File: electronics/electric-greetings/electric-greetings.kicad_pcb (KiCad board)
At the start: 2 copper layers, 12 x 30 mm, 17 parts, among them Q1 ALS-PT19-315C, SW1 B3U-1000P_SPST-NO_SMD, U1 ATSAMD21E18A, U2 AP2112K-3.3, U3 APA102-2020

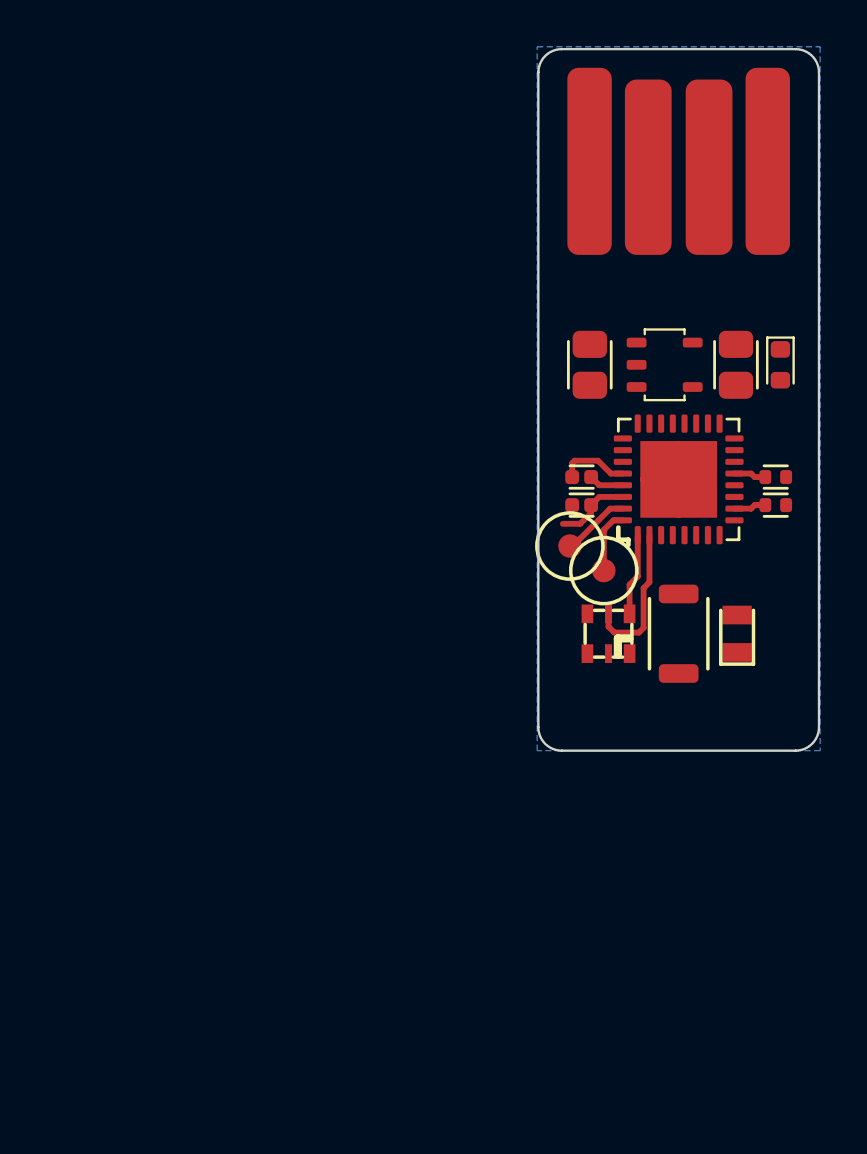
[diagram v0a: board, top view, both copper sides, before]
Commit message: Schematic tweaks, placement changes, routing
Most routing done, added capacitive buttons, remapped micro pins slightly.
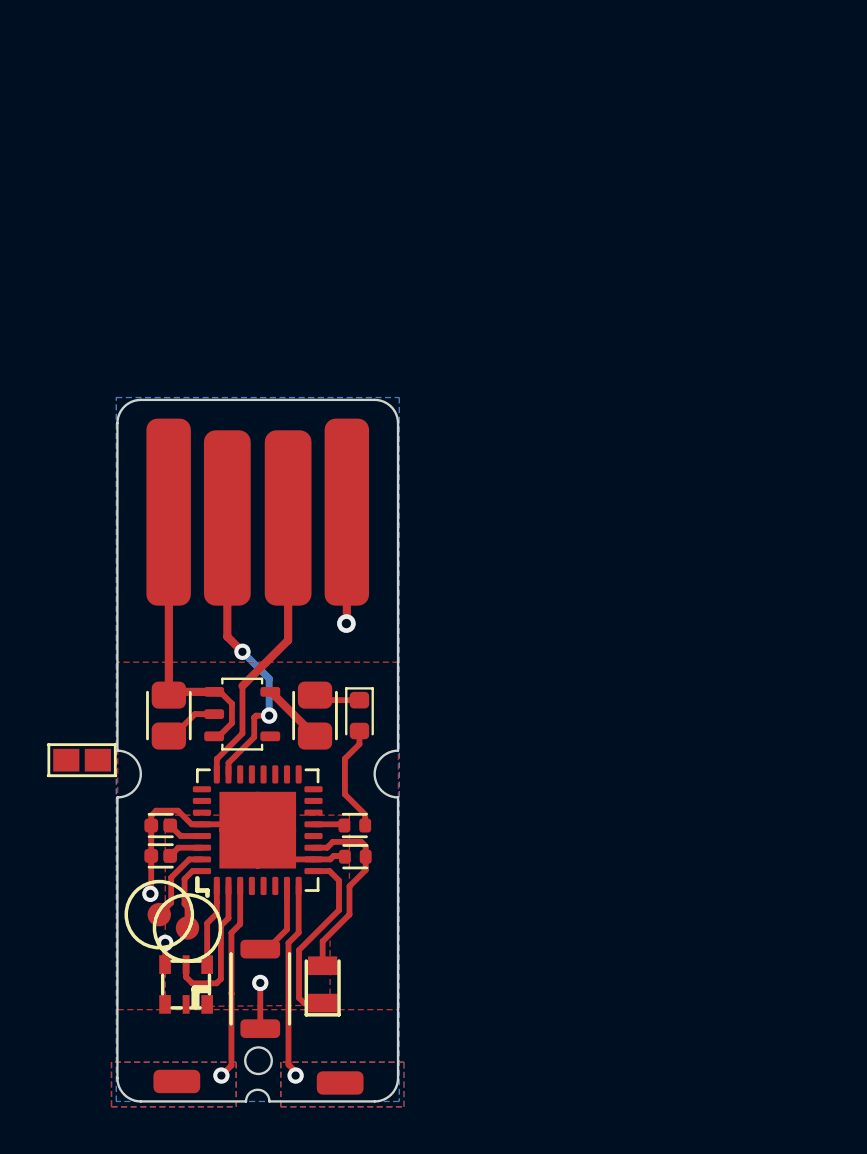
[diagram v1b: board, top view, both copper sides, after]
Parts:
- added P1: PAD_SOLDER_2mm, Applidyne_Connector:PAD_SOLDER_2mm, F.Cu at (102.5, 99.1)
- added P2: PAD_SOLDER_2mm, Applidyne_Connector:PAD_SOLDER_2mm, F.Cu at (109.5, 99.2)
- added SL1: SOLDER-LINK-2, Applidyne_Link:SJ1608-2N, F.Cu at (98.5, 85.4)
- moved LOGO1 24.2 mm to (106.0, 89.2)
- moved TEST1 23.6 mm to (101.8, 92.0)
- moved U3 23.5 mm to (102.9, 95.0)
- moved SW1 23.5 mm to (106.1, 95.2), turned to 270 degrees
- moved TEST2 23.5 mm to (103.0, 92.6)
- moved U2 23.4 mm to (105.3, 83.4)
- moved R2 23.4 mm to (110.2, 89.5)
- moved C1 23.4 mm to (101.8, 89.5)
- moved C3 23.4 mm to (102.2, 83.5)
- moved C4 23.4 mm to (108.5, 83.5), turned to 90 degrees
- moved D1 23.4 mm to (110.3, 83.5)
- moved J?1 23.4 mm to (106.0, 69.9)
- moved LOGO4 23.4 mm to (106.0, 74.8)
- moved U1 23.4 mm to (106.0, 88.4)
- moved C2 23.4 mm to (101.8, 88.2)
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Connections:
- SW1 pad 2: RESET -> USER_BUTTON
- U1 pad : (no net) -> GND
- U1 pad 11: Net-(U1-Pad11) -> PHOTOSENSOR
- U1 pad 3: Net-(U1-Pad3) -> TOUCH_A
- U1 pad 7: PHOTOSENSOR -> USER_BUTTON
- U1 pad 8: CURRENT -> TOUCH_B
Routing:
- net GND: track 4.42 -> 23.0 mm, vias 0 -> 4
- net USB_D-: track 0.00 -> 12.8 mm, vias 0 -> 2
- net VCC: track 0.00 -> 12.7 mm
- net USB_D+: track 0.00 -> 12.2 mm
- net +3.3V: track 3.24 -> 12.7 mm
- net TOUCH_A: track 0.00 -> 8.46 mm, vias 0 -> 1
- net TOUCH_B: track 0.00 -> 8.41 mm, vias 0 -> 1
- net PHOTOSENSOR: track 0.00 -> 8.28 mm
- net Net-(D1-PadA): track 0.00 -> 4.66 mm
- net USER_BUTTON: track 0.00 -> 3.35 mm
- net SWD_CLK: track 2.93 -> 3.43 mm
- added copper zone on F.Cu, net +3.3V
- added copper zone on B.Cu, net TOUCH_A
- added copper zone on F.Cu, net TOUCH_A
- added copper zone on B.Cu, net TOUCH_B
- added copper zone on F.Cu, net TOUCH_B
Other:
- outline, holes or cut-outs redrawn

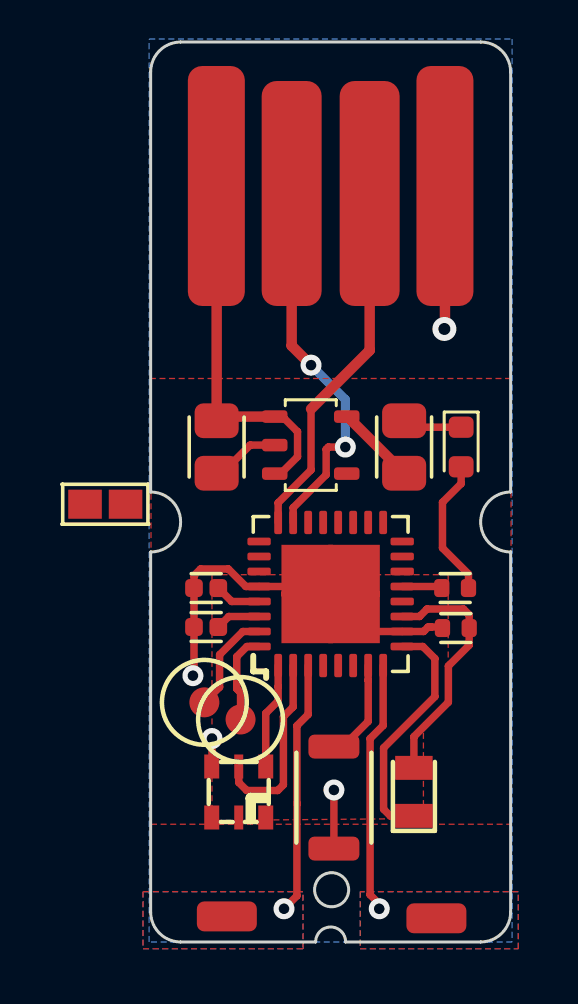
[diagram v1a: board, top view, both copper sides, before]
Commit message: More minor tweaks, finished all routing
Most cosmetics finished, just iterating on useless details now
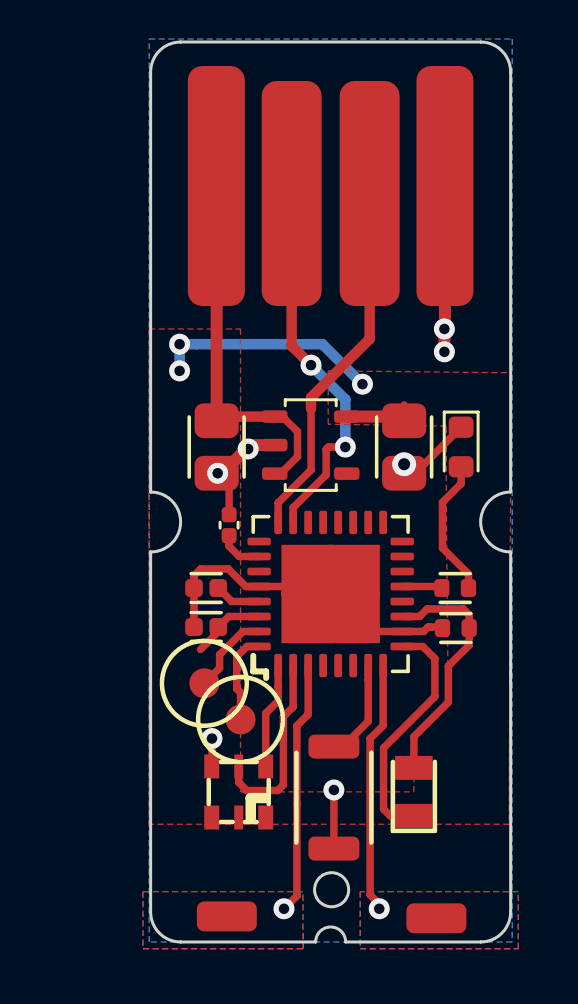
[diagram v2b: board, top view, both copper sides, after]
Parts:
- SL1: value SOLDER-LINK-2 -> SOLDER-LINK-2-TINY; footprint Applidyne_Link:SJ1608-2N -> Applidyne_Link:SJ1005-2N
- moved SL1 4.19 mm to (102.6, 86.1), turned to 270 degrees
- moved TEST1 0.64 mm to (101.8, 91.4)
- turned C4 to 270 degrees
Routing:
- net +3.3V: track 12.7 -> 21.1 mm, vias 0 -> 3
- net GND: track 23.0 -> 27.5 mm, vias 4 -> 7
- net RESET: track 0.00 -> 1.49 mm
- net SWD_CLK: track 3.43 -> 2.80 mm

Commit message: Removed usb logo
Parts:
- removed LOGO4: LOGO, Applidyne_Logo:USB_LOGO410X250
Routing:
- net GND: track 27.5 -> 30.1 mm, vias 7 -> 8
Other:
- board text added: "eui.io"
- board text removed: "try.eui.io"

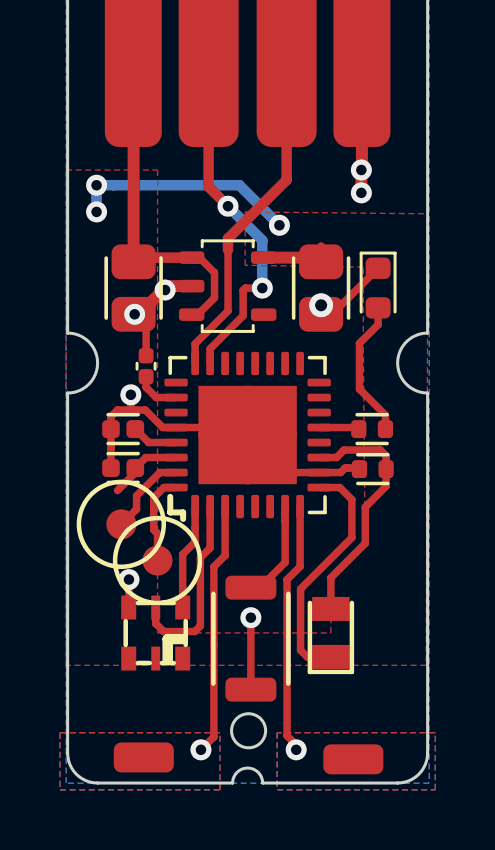
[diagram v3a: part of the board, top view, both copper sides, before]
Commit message: Fixed SWD programming points with 1mm pad footprint
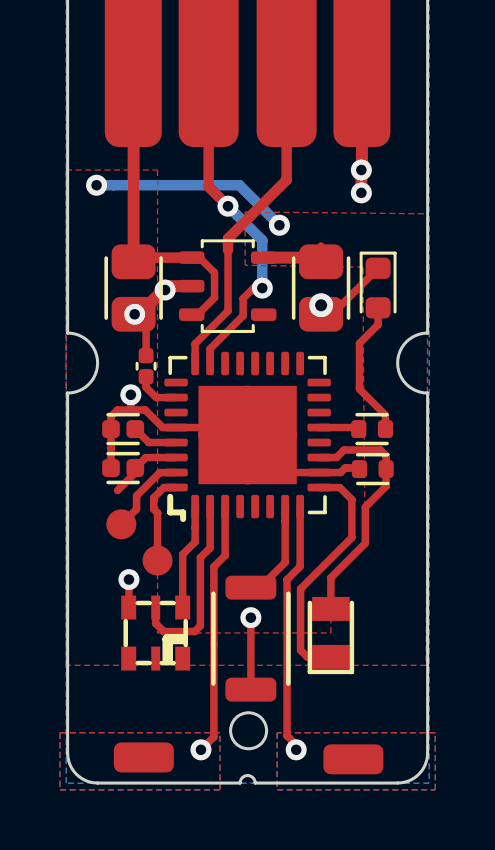
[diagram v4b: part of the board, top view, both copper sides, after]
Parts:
- TEST1, TEST2: footprint Applidyne_Test:TP200 -> Applidyne_Test:TP100
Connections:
- U1 pad : GND -> (no net)
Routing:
- net +3.3V: track 21.1 -> 20.2 mm, vias 3 -> 2
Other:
- outline, holes or cut-outs redrawn
- board text added: "."

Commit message: Manufacturing files generated
Exported gerbers, generated PDF's.
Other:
- board text added: "2 Layer Stackup 2.0mm FR4 1oz (35um) copper ENIG surface finish Matte black soldermask 12x30mm outline. 0.35mm via drill NO silkscreen on top & bottom Plate edge around capacitive touch pads as marked. Inflate soldermask as required."
- board text added: "A"
- board text added: "B"
- board text added: "Capacitive Buttons Plate board edge"
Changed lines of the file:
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@@
   (general
     (thickness 2)
-    (drawings 23)
+    (drawings 31)
     (tracks 160)
     (zones 0)
@@
     (visible_elements FFFFFF7F)
     (pcbplotparams
-      (layerselection 0x010fc_ffffffff)
-      (usegerberextensions false)
+      (layerselection 0x213cc_ffffffff)
+      (usegerberextensions true)
       (usegerberattributes false)
       (usegerberadvancedattributes false)
@@
       (outputformat 1)
       (mirror false)
-      (drillshape 1)
+      (drillshape 0)
       (scaleselection 1)
-      (outputdirectory ""))
+      (outputdirectory "Outputs/Gerbers/"))
   )
   (net 0 "")
@@
     )
   )
+  (gr_line (start 112 98.5) (end 113 98.5) (layer Cmts.User) (width 0.2))
+  (gr_line (start 107 100) (end 107 100.5) (layer Cmts.User) (width 0.2))
+  (gr_line (start 105 100) (end 105 100.5) (layer Cmts.User) (width 0.2))
+  (gr_line (start 100 98.5) (end 99 98.5) (layer Cmts.User) (width 0.2))
+  (gr_text B (at 109.5 103) (layer Cmts.User)
+    (effects (font (size 1.5 1.5) (thickness 0.3)))
+  )
+  (gr_text A (at 102.5 103) (layer Cmts.User)
+    (effects (font (size 1.5 1.5) (thickness 0.3)))
+  )
+  (gr_text "Capacitive Buttons\nPlate board edge" (at 106.5 109.5) (layer Cmts.User)
+    (effects (font (size 1.5 1.5) (thickness 0.3)))
+  )
+  (gr_text "2 Layer Stackup\n\n2.0mm FR4\n1oz (35um) copper\nENIG surface finish\nMatte black soldermask\n12x30mm outline.\n0.35mm via drill\n\nNO silkscreen on top & bottom\nPlate edge around capacitive touch pads as marked.\nInflate soldermask as required.\n" (at 140.5 84.5) (layer Cmts.User)
+    (effects (font (size 2 2) (thickness 0.3)) (justify left))
+  )
   (gr_text . (at 110.6 91.2 90) (layer F.Mask)
